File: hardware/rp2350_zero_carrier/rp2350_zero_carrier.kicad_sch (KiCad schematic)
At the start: 8 parts, among them J1 RP2350-Zero_Header(23pin,GPIO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, J2 USB-A_Host(Neltron_5075AR-04-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, SW1 1回路2接点スイッチ(3pin,NKK_115643,ON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, SW2 1回路2接点スイッチ(3pin,NKK_115643,ON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, SW3 1回路2接点スイッチ(3pin,NKK_115643,ON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

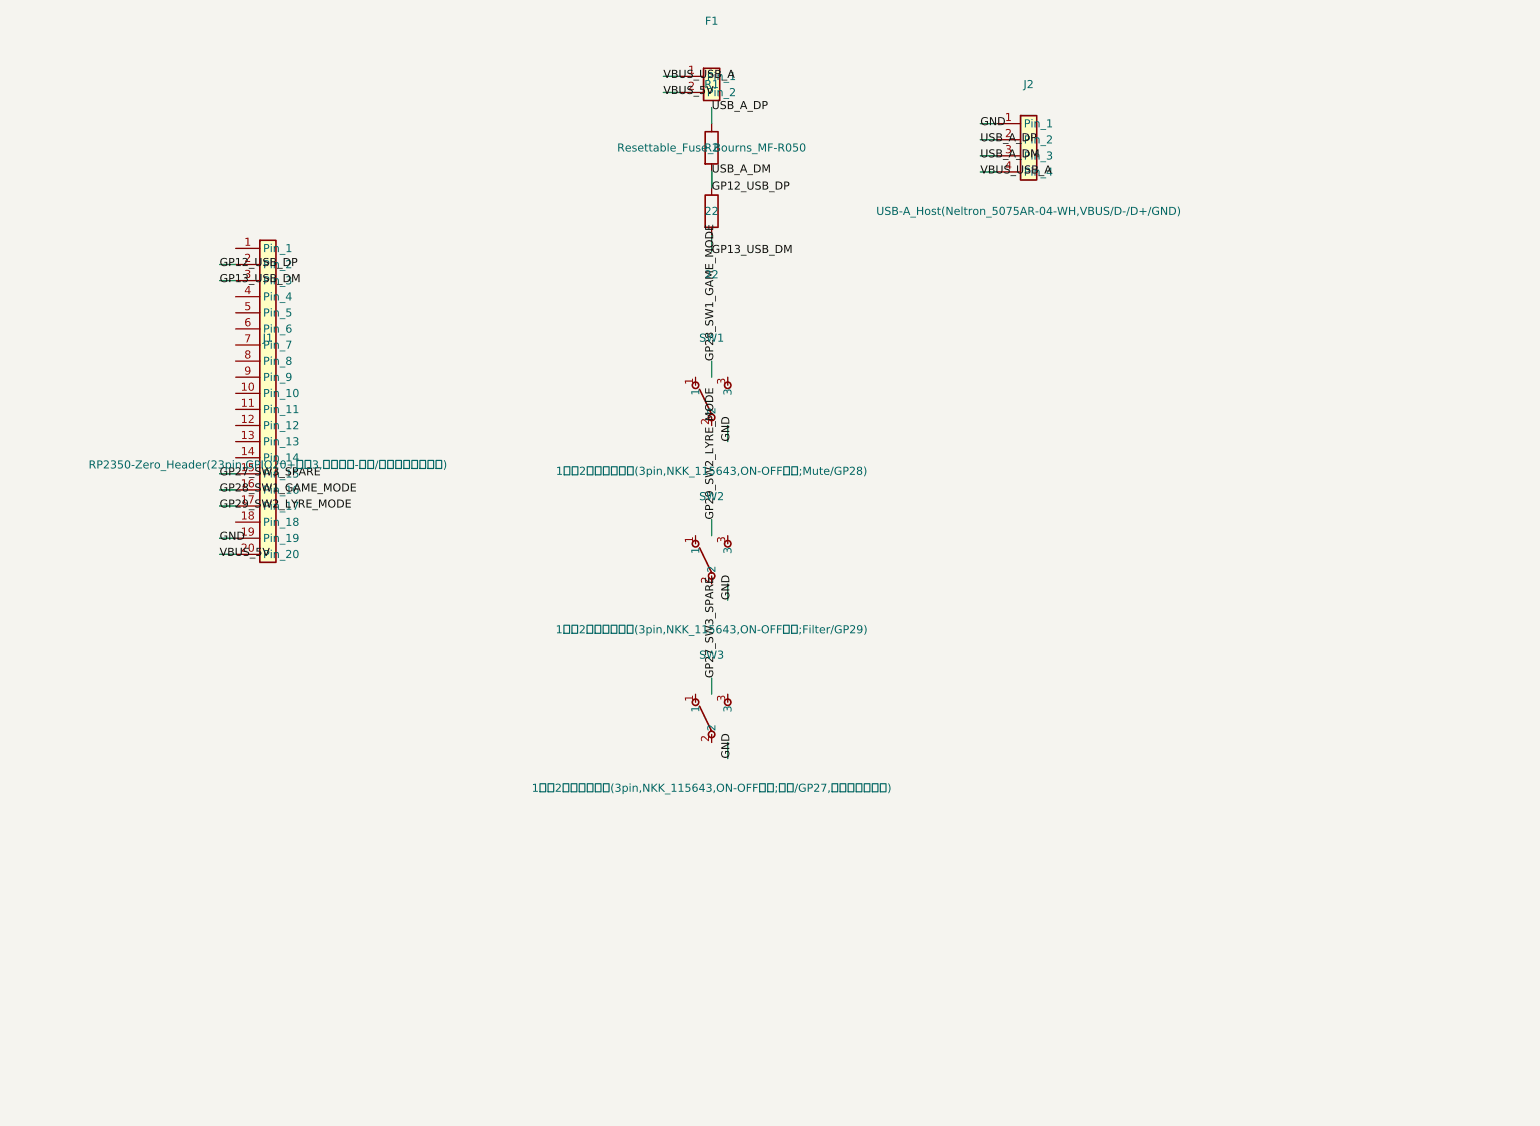
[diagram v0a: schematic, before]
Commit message: SW4(USB-A VBUS電源スイッチ)を回路図に追加
RP2350-Zeroの5V -> F1(ヒューズ) -> SW4 -> J2(USB-A)pin1(VBUS) の直列経路に
SW4を割り込ませた。SW1-3と同じSwitch:SW_SPDTシンボル・footprint
(SW_SPDT_NKK_115643_Slide)を流用し、中央コモンをF1側(VBUS_USB_A net)、
片側接点をJ2側(新設のVBUS_USB_A_SW net)に接続、残り1接点はNC。GPIOには
接続しない純粋な電源スイッチ。GND等の他配線は変更なし。

Co-Authored-By: Claude Sonnet 5 <noreply@anthropic.com>
Claude-Session: https://claude.ai/code/session_01E7QH5gCzZj3tVha83XRuUt
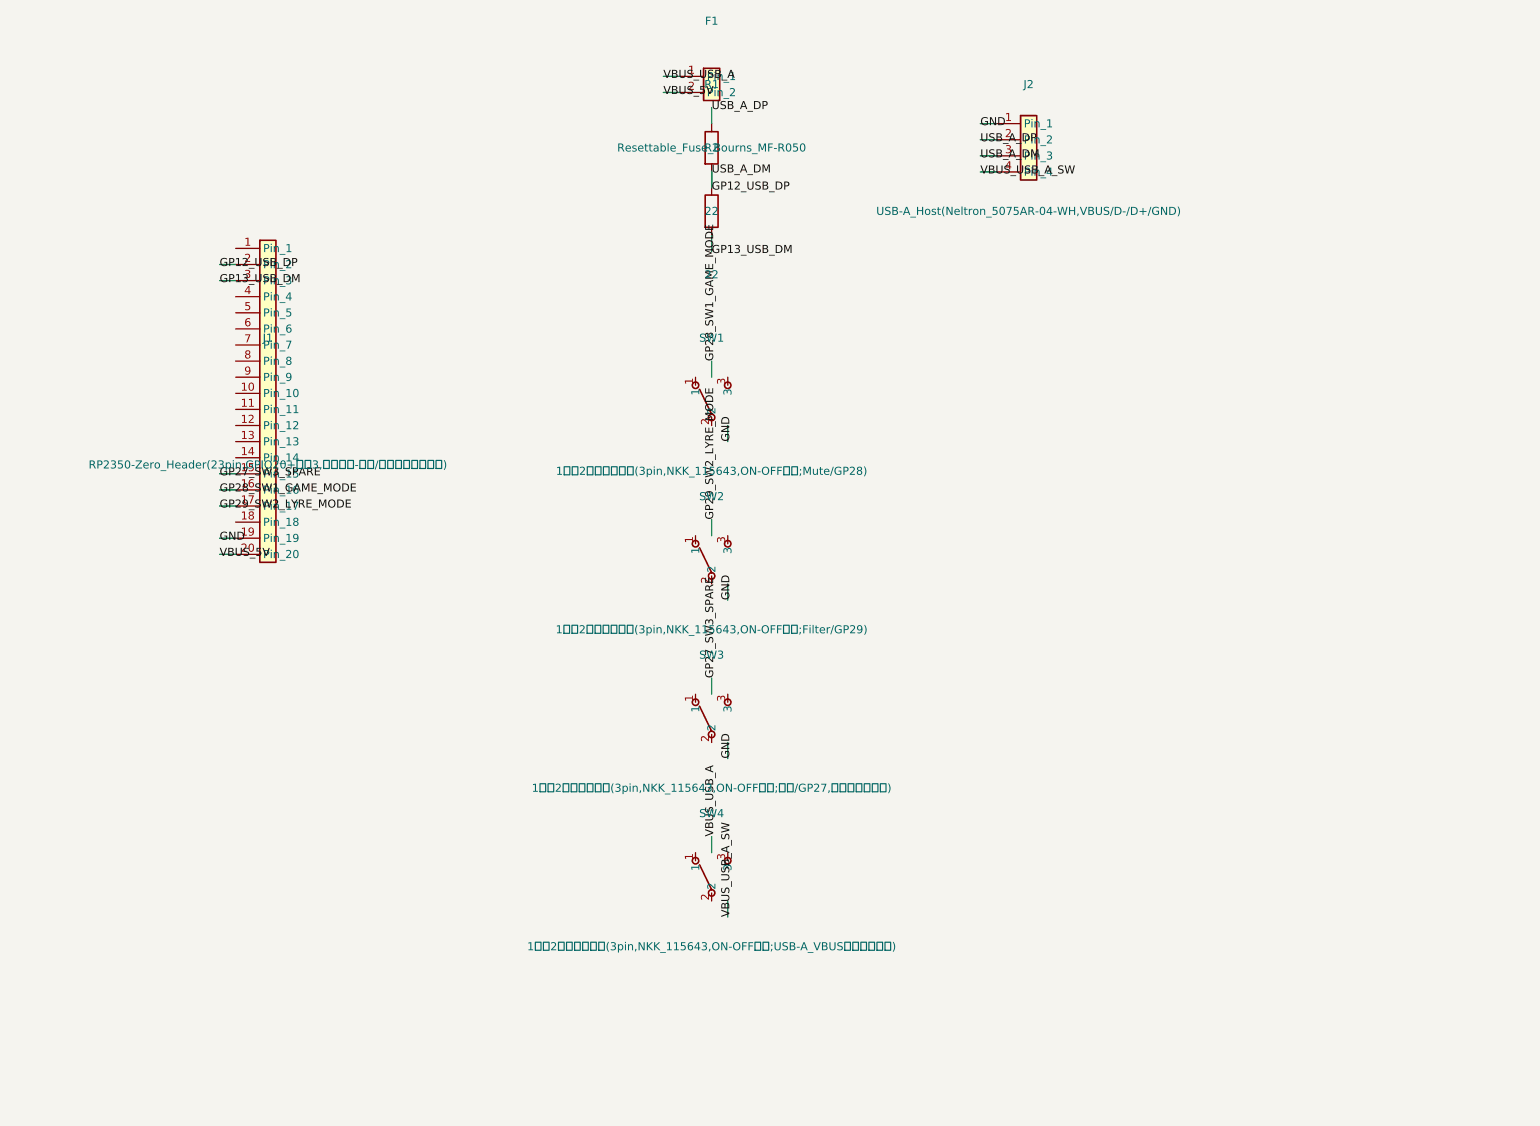
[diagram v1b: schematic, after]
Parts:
- added SW4: 1回路2接点スイッチ(3pin,NKK_115643,ON-OFF用途;USB-A_VBUS電源ス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, rp2350_zero_carrier:SW_SPDT_NKK_115643_Slide, symbol Switch:SW_SPDT
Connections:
- net VBUS_USB_A: no longer J2.4 (Pin_4)
- new net VBUS_USB_A_SW: J2.4 (Pin_4)
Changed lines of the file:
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@@
+    )
+  )
+  (symbol (lib_id "Switch:SW_SPDT") (at 110 205 0) (unit 1)
+    (in_bom yes) (on_board yes) (dnp no) (fields_autoplaced yes)
+    (property "Reference" "SW4" (at 110 195 0) (effects (font (size 1.27 1.27))))
+    (property "Value" "1回路2接点スイッチ(3pin,NKK_115643,ON-OFF用途;USB-A_VBUS電源スイッチ)" (at 110 216 0) (effects (font (size 1.27 1.27))))
+    (property "Footprint" "rp2350_zero_carrier:SW_SPDT_NKK_115643_Slide" (at 110 205 0) (effects (font (size 1.27 1.27)) hide))
+    (property "Datasheet" "" (at 110 205 0) (effects (font (size 1.27 1.27)) hide))
+    (pin "1")
+    (pin "2")
+    (pin "3")
+    (instances
+      (project "rp2350_zero_carrier"
+        (path "/"
+          (reference "SW4") (unit 1)
+        )
+      )
     )
   )
@@
   (wire (pts (xy 110 176.19) (xy 110 173.65)) (stroke (width 0) (type default)))
   (wire (pts (xy 112.54 183.81) (xy 112.54 186.35)) (stroke (width 0) (type default)))
+  (wire (pts (xy 110 201.19) (xy 110 198.65)) (stroke (width 0) (type default)))
+  (wire (pts (xy 112.54 208.81) (xy 112.54 211.35)) (stroke (width 0) (type default)))
   (label "VBUS_5V" (at 32.38 154.13 0) (effects (font (size 1.27 1.27)) (justify left)))
   (label "GND" (at 32.38 151.59 0) (effects (font (size 1.27 1.27)) (justify left)))
@@
   (label "VBUS_5V" (at 102.38 81.27 0) (effects (font (size 1.27 1.27)) (justify left)))
   (label "VBUS_USB_A" (at 102.38 78.73 0) (effects (font (size 1.27 1.27)) (justify left)))
-  (label "VBUS_USB_A" (at 152.38 93.81 0) (effects (font (size 1.27 1.27)) (justify left)))
+  (label "VBUS_USB_A_SW" (at 152.38 93.81 0) (effects (font (size 1.27 1.27)) (justify left)))
   (label "USB_A_DM" (at 152.38 91.27 0) (effects (font (size 1.27 1.27)) (justify left)))
   (label "USB_A_DP" (at 152.38 88.73 0) (effects (font (size 1.27 1.27)) (justify left)))
@@
   (label "GP27_SW3_SPARE" (at 110 173.65 90) (effects (font (size 1.27 1.27)) (justify left)))
   (label "GND" (at 112.54 186.35 90) (effects (font (size 1.27 1.27)) (justify left)))
+  (label "VBUS_USB_A" (at 110 198.65 90) (effects (font (size 1.27 1.27)) (justify left)))
+  (label "VBUS_USB_A_SW" (at 112.54 211.35 90) (effects (font (size 1.27 1.27)) (justify left)))
   (sheet_instances
     (path "/" (page "1"))

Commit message: J3(2個目のRP2350-Zero、ボード2役割)を回路図に追加
serial_midi_device(UARTミラー→USB-MIDIブリッジ)を別基板ではなく同一
PCB上の2個目のRP2350-Zeroソケットとして同居させる。J3はJ1と全く同じ
footprint(RP2350_Zero_Header_23p)・ピン配置表を再利用。

J1のGP4(UART1 TX、既存ミラー出力)とJ3のGP5(UART1 RX、serial_midi_device
既定ピン)を新規ネット UART_MIRROR で基板内直結。GNDは既存の共通GND netに
J3のpin2を追加するだけで足りる(README §7の「GP4->GP5、GND->GND」のうち
GND分は既存の共有netで自動的に満たされる)。J3はUSB-Aホストもスイッチも
持たず、5V/3V3等の未使用ピンはNC(各RP2350-Zeroは自分のUSB-Cから独立して
給電される想定)。

Co-Authored-By: Claude Sonnet 5 <noreply@anthropic.com>
Claude-Session: https://claude.ai/code/session_01E7QH5gCzZj3tVha83XRuUt
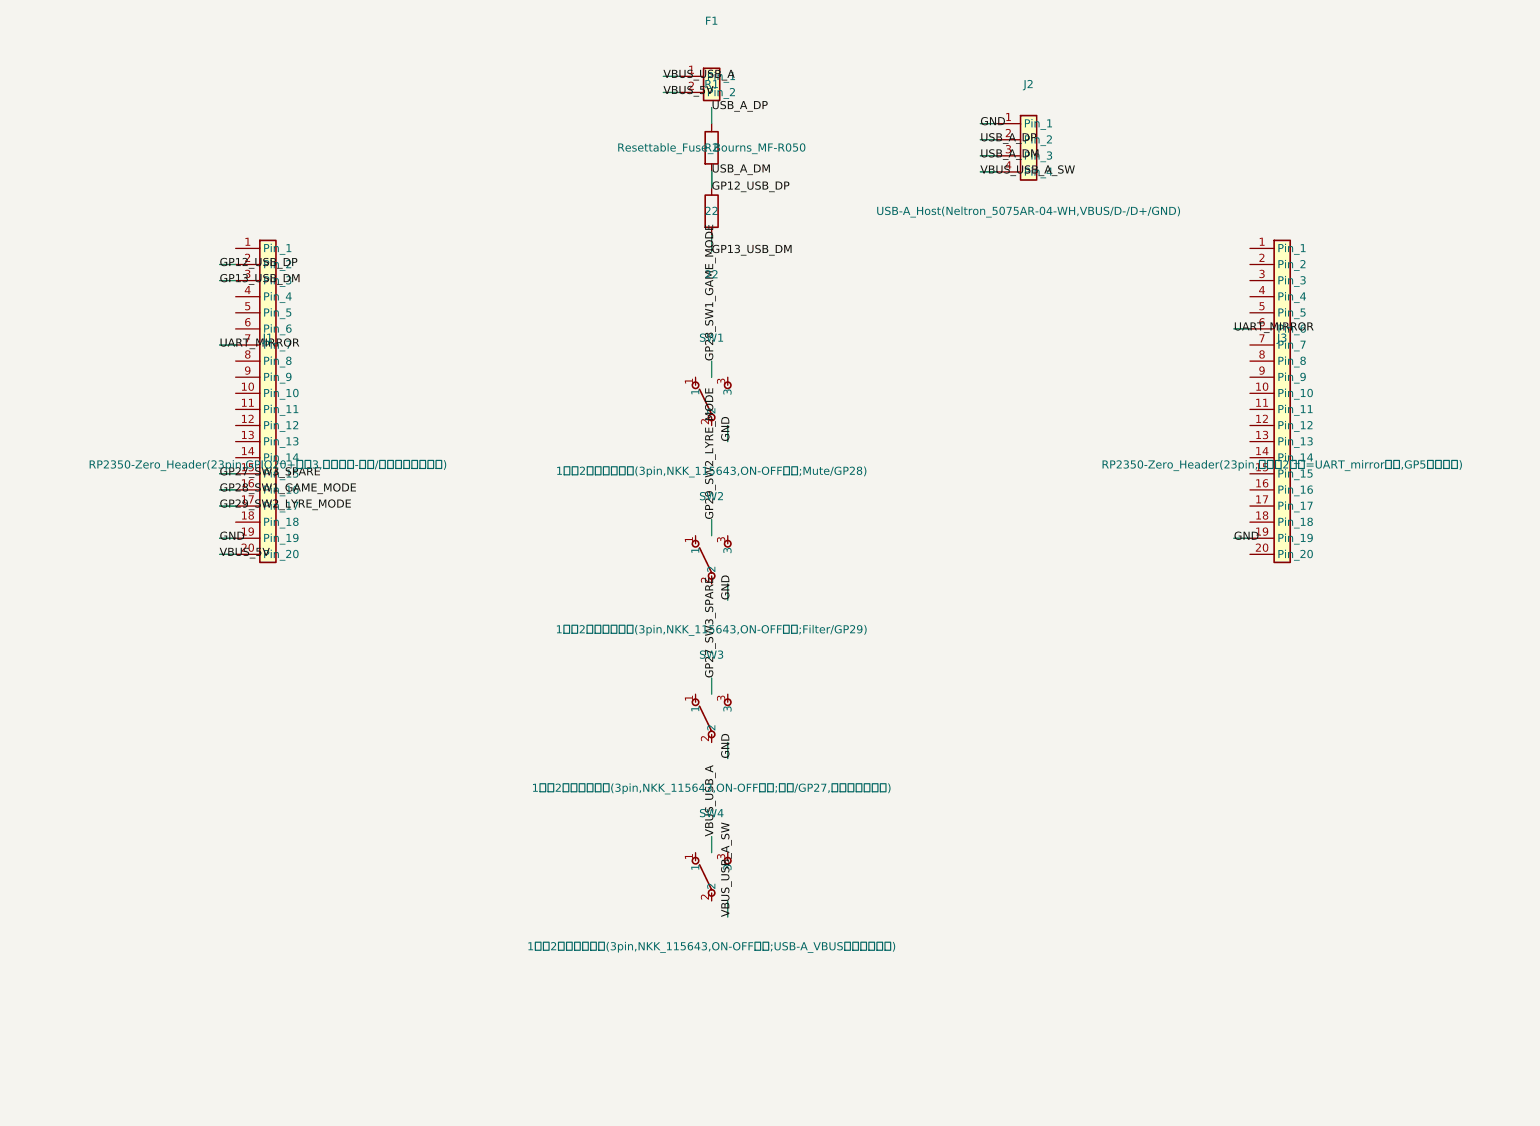
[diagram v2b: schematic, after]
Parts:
- added J3: RP2350-Zero_Header(23pin,ボード2役割=UART_mirror受信,GP5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, rp2350_zero_carrier:RP2350_Zero_Header_23p, symbol Connector_Generic:Conn_01x20
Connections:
- net GND: now also J3.19 (Pin_19)
- net UART_MIRROR: now reaches J1.7 (Pin_7)
- net UART_MIRROR: now also J3.6 (Pin_6)
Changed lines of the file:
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@@
+    )
+  )
+  (symbol (lib_id "Connector_Generic:Conn_01x20") (at 200 130 0) (unit 1)
+    (in_bom yes) (on_board yes) (dnp no) (fields_autoplaced yes)
+    (property "Reference" "J3" (at 200 120 0) (effects (font (size 1.27 1.27))))
+    (property "Value" "RP2350-Zero_Header(23pin,ボード2役割=UART_mirror受信,GP5のみ使用)" (at 200 140 0) (effects (font (size 1.27 1.27))))
+    (property "Footprint" "rp2350_zero_carrier:RP2350_Zero_Header_23p" (at 200 130 0) (effects (font (size 1.27 1.27)) hide))
+    (property "Datasheet" "" (at 200 130 0) (effects (font (size 1.27 1.27)) hide))
+    (pin "1")
+    (pin "2")
+    (pin "3")
+    (pin "4")
+    (pin "5")
+    (pin "6")
+    (pin "7")
+    (pin "8")
+    (pin "9")
+    (pin "10")
+    (pin "11")
+    (pin "12")
+    (pin "13")
+    (pin "14")
+    (pin "15")
+    (pin "16")
+    (pin "17")
+    (pin "18")
+    (pin "19")
+    (pin "20")
+    (instances
+      (project "rp2350_zero_carrier"
+        (path "/"
+          (reference "J3") (unit 1)
+        )
+      )
     )
   )
@@
   (wire (pts (xy 34.92 110.95) (xy 32.38 110.95)) (stroke (width 0) (type default)))
   (wire (pts (xy 34.92 108.41) (xy 32.38 108.41)) (stroke (width 0) (type default)))
+  (wire (pts (xy 34.92 121.11) (xy 32.38 121.11)) (stroke (width 0) (type default)))
+  (wire (pts (xy 194.92 151.59) (xy 192.38 151.59)) (stroke (width 0) (type default)))
+  (wire (pts (xy 194.92 118.57) (xy 192.38 118.57)) (stroke (width 0) (type default)))
   (wire (pts (xy 110 93.81) (xy 110 96.35)) (stroke (width 0) (type default)))
   (wire (pts (xy 110 86.19) (xy 110 83.65)) (stroke (width 0) (type default)))
@@
   (label "VBUS_USB_A" (at 110 198.65 90) (effects (font (size 1.27 1.27)) (justify left)))
   (label "VBUS_USB_A_SW" (at 112.54 211.35 90) (effects (font (size 1.27 1.27)) (justify left)))
+  (label "UART_MIRROR" (at 32.38 121.11 0) (effects (font (size 1.27 1.27)) (justify left)))
+  (label "GND" (at 192.38 151.59 0) (effects (font (size 1.27 1.27)) (justify left)))
+  (label "UART_MIRROR" (at 192.38 118.57 0) (effects (font (size 1.27 1.27)) (justify left)))
   (sheet_instances
     (path "/" (page "1"))
